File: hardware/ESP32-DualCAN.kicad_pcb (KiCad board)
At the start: 2 copper layers, 38.8 x 19.6 mm, 28 parts, among them J1 Molex 70553 6p, J2 Conn_01x10_Socket, J3 Conn_01x10_Socket, J4 holes, J5 pads, J6 holes, J7 pads, U1 LV2862Y, U2 ESP32-C6-SuperMini, U3 TCAN1044AV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

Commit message: fix: flipped VehicleCAN pins
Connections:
- J1 pad 5: CAN0_H -> CAN0_L
- J1 pad 6: CAN0_L -> CAN0_H
- J4 pad 5: CAN0_H -> CAN0_L
- J4 pad 6: CAN0_L -> CAN0_H
- J5 pad 5: CAN0_H -> CAN0_L
- J5 pad 6: CAN0_L -> CAN0_H
- J6 pad 5: CAN0_H -> CAN0_L
- J6 pad 6: CAN0_L -> CAN0_H
- J7 pad 5: CAN0_H -> CAN0_L
- J7 pad 6: CAN0_L -> CAN0_H
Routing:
- net CAN0_H: track 25.6 -> 30.6 mm
- net GND: track 63.1 -> 67.0 mm
- net CAN0_L: track 29.6 -> 26.4 mm
- added copper zone on F.Cu, net +5V
- removed copper zone on F.Cu, net +3.3V
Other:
- board text added: "Vin G 1L 1H 0L 0H"
- board text removed: "Vin G 1L 1H 0H 0L"

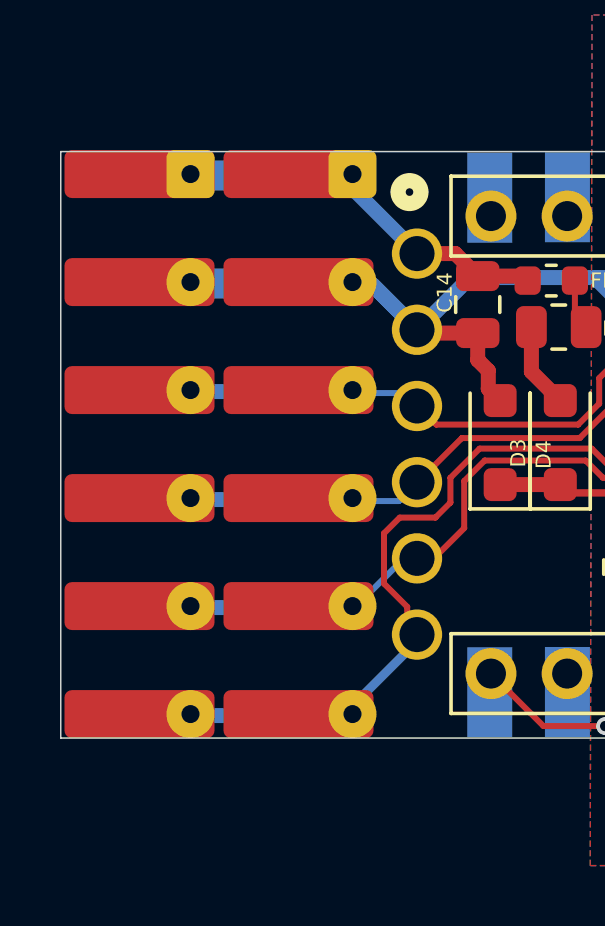
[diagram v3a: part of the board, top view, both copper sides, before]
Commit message: can silk on top
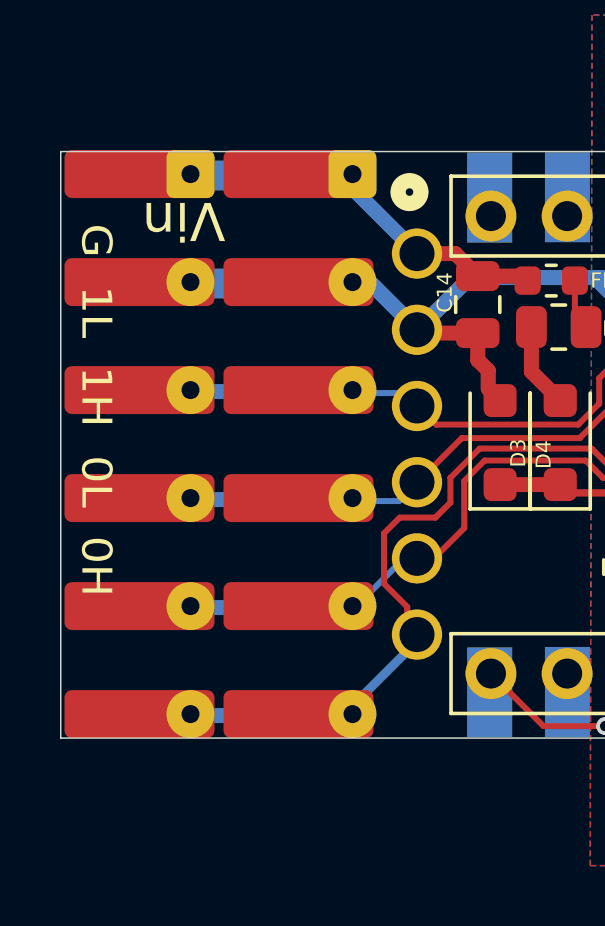
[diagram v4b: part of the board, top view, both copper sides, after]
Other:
- board text added: "G 1L 1H 0L 0H"
- board text added: "Vin"
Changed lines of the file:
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@@
+		)
+	)
+	(gr_text "G  1L  1H  0L  0H"
+		(at 122.25 83.25 270)
+		(layer "F.SilkS")
+		(effects
+			(font
+				(size 1 1.07)
+				(thickness 0.15)
+			)
+			(justify left bottom)
+		)
+	)
+	(gr_text "Vin"
+		(at 125.75 83.15 180)
+		(layer "F.SilkS")
+		(effects
+			(font
+				(size 1.27 1.27)
+			)
 		)
 	)
